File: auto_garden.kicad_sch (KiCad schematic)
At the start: 22 parts, among them M1 Pump, U1 LM358, U2 LM358, U3 LM358

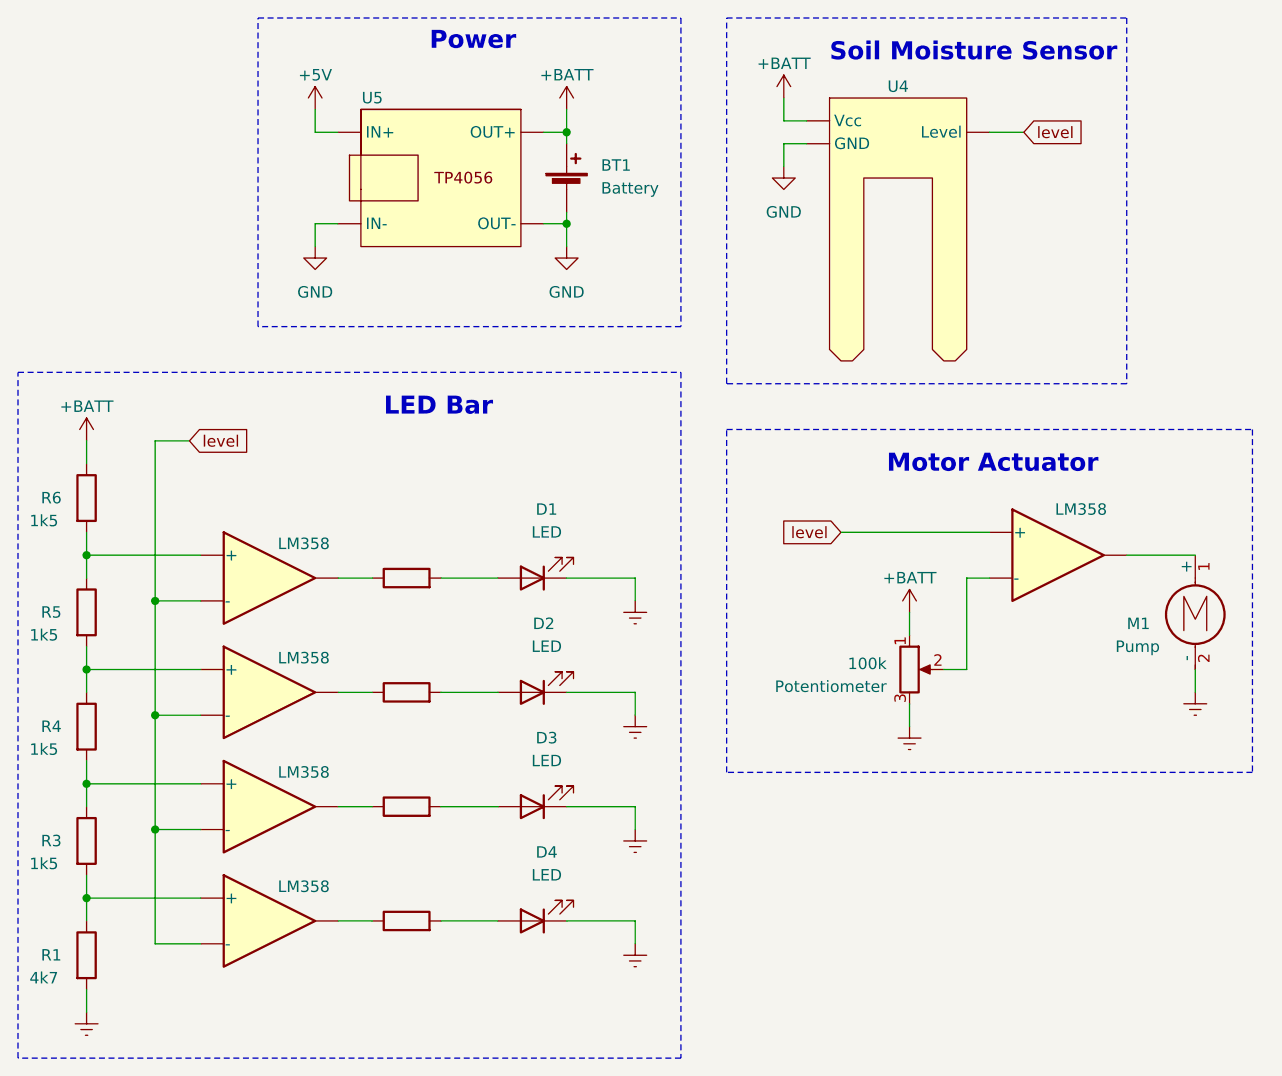
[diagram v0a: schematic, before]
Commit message: add mosfet
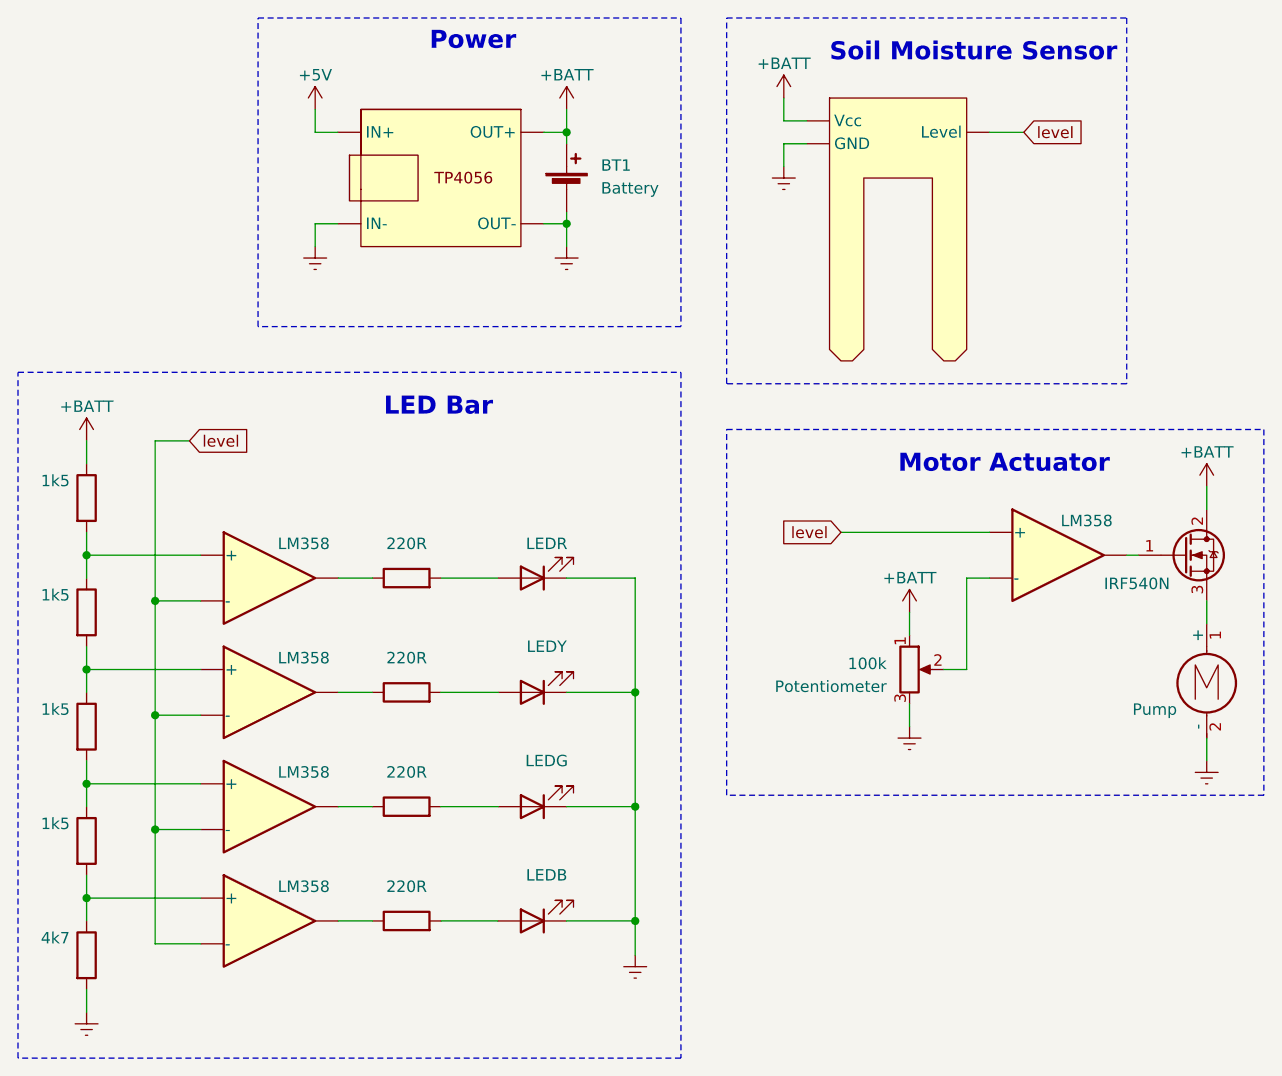
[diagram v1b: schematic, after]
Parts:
- added Q1: IRF540N, Package_TO_SOT_THT:TO-220-3_Vertical, symbol Transistor_FET:IRF540N
- D1: value LED -> LEDR
- D2: value LED -> LEDY
- D3: value LED -> LEDG
- D4: value LED -> LEDB
- R: value R -> 220R
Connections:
- net +BATT: now also Q1.2 (D)
- net Earth: now also BT1.2 (-), U4. (Vcc), U5. (OUT-)
- net at U1.1: now also Q1.1 (G); no longer M1.1 (+)
- removed net GND: BT1.2 (-), U4. (Vcc), U5. (OUT-)
- new net: M1.1 (+), Q1.3 (S)
